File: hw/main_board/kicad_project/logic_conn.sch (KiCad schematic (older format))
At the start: 12 parts, among them P6 CONN_20X2, P8 CONN_12, U8 MAX3002, U9 MAX3002

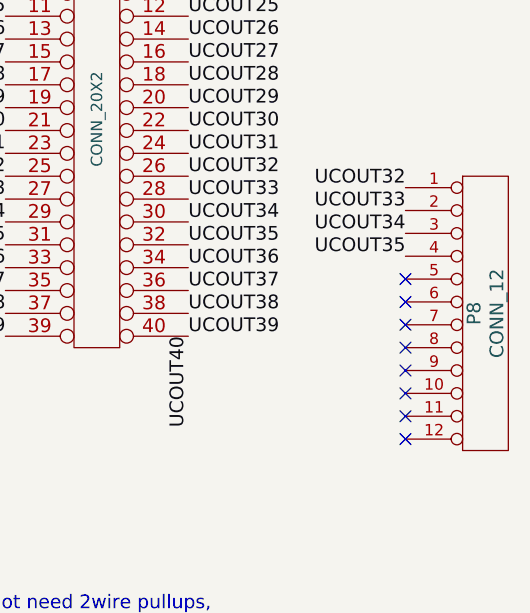
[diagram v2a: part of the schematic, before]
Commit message: final rework of mux board, finalizing stacking connectors, almost there
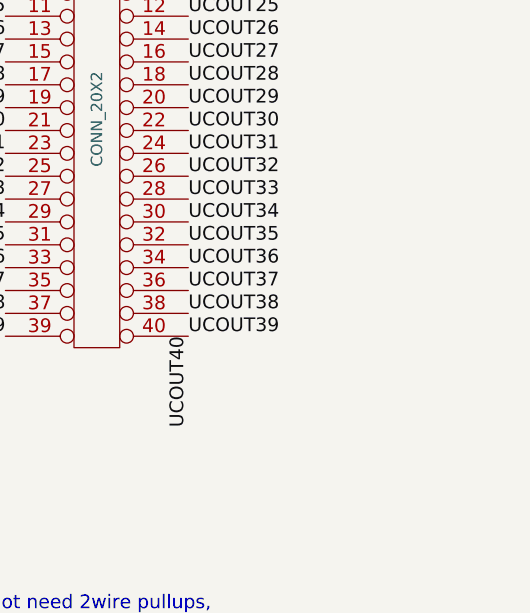
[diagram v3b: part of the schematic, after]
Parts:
- removed P8: CONN_12, symbol CONN_12
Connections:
- no-connect marks 14 -> 6
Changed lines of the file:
@@
 EESchema Schematic File Version 2
-LIBS:power
-LIBS:device
-LIBS:transistors
-LIBS:conn
-LIBS:linear
-LIBS:regul
-LIBS:74xx
-LIBS:cmos4000
-LIBS:adc-dac
-LIBS:memory
-LIBS:xilinx
-LIBS:special
-LIBS:microcontrollers
-LIBS:dsp
-LIBS:microchip
-LIBS:analog_switches
-LIBS:motorola
-LIBS:texas
-LIBS:intel
-LIBS:audio
-LIBS:interface
-LIBS:digital-audio
-LIBS:philips
-LIBS:display
-LIBS:cypress
-LIBS:siliconi
-LIBS:opto
-LIBS:atmel
-LIBS:contrib
-LIBS:valves
 LIBS:ddslib
-LIBS:demuxcomplib
-LIBS:tdsc-kicad-convert
 LIBS:tDCS_driver-cache
 EELAYER 24 0
@@
 $EndComp
 $Comp
-L DVDD_2V5 #PWR08
+L DVDD_2V5 #PWR014
 U 1 1 5245D941
 P 3300 4300
-F 0 "#PWR08" H 3300 4400 30  0001 C CNN
+F 0 "#PWR014" H 3300 4400 30  0001 C CNN
 F 1 "DVDD_2V5" H 3300 4410 30  0000 C CNN
 F 2 "" H 3300 4300 60  0001 C CNN
@@
 $EndComp
 $Comp
-L AGND #PWR09
+L AGND #PWR015
 U 1 1 5245D93C
 P 3000 4650
-F 0 "#PWR09" H 3000 4650 40  0001 C CNN
+F 0 "#PWR015" H 3000 4650 40  0001 C CNN
 F 1 "AGND" H 3000 4580 50  0000 C CNN
 F 2 "" H 3000 4650 60  0001 C CNN
@@
 $EndComp
 $Comp
-L DGND #PWR010
+L DGND #PWR016
 U 1 1 5245D93B
 P 3950 4650
-F 0 "#PWR010" H 3950 4650 40  0001 C CNN
+F 0 "#PWR016" H 3950 4650 40  0001 C CNN
 F 1 "DGND" H 3950 4580 40  0000 C CNN
 F 2 "" H 3950 4650 60  0001 C CNN
@@
 $EndComp
 $Comp
-L AGND #PWR011
+L AGND #PWR017
 U 1 1 5245D93A
 P 3500 2700
-F 0 "#PWR011" H 3500 2700 40  0001 C CNN
+F 0 "#PWR017" H 3500 2700 40  0001 C CNN
 F 1 "AGND" H 3500 2630 50  0000 C CNN
 F 2 "" H 3500 2700 60  0001 C CNN
@@
 $EndComp
 $Comp
-L DVDD_3V3 #PWR012
+L DVDD_3V3 #PWR018
 U 1 1 5245D939
 P 4500 4200
-F 0 "#PWR012" H 4500 4300 30  0001 C CNN
+F 0 "#PWR018" H 4500 4300 30  0001 C CNN
 F 1 "DVDD_3V3" H 4500 4310 30  0000 C CNN
 F 2 "" H 4500 4200 60  0001 C CNN
@@
 MUXC[0..4]
 $Comp
-L DVDD_3V3 #PWR013
+L DVDD_3V3 #PWR019
 U 1 1 523C1EE9
 P 4450 1000
-F 0 "#PWR013" H 4450 1100 30  0001 C CNN
+F 0 "#PWR019" H 4450 1100 30  0001 C CNN
 F 1 "DVDD_3V3" H 4450 1110 30  0000 C CNN
 F 2 "" H 4450 1000 60  0001 C CNN
@@
 $EndComp
 $Comp
-L AGND #PWR014
+L AGND #PWR020
 U 1 1 523C1EBE
 P 3500 2450
-F 0 "#PWR014" H 3500 2450 40  0001 C CNN
+F 0 "#PWR020" H 3500 2450 40  0001 C CNN
 F 1 "AGND" H 3500 2380 50  0000 C CNN
 F 2 "" H 3500 2450 60  0001 C CNN
@@
 $EndComp
 $Comp
-L DGND #PWR015
+L DGND #PWR021
 U 1 1 523C1EBD
 P 3900 550
-F 0 "#PWR015" H 3900 550 40  0001 C CNN
+F 0 "#PWR021" H 3900 550 40  0001 C CNN
 F 1 "DGND" H 3900 480 40  0000 C CNN
 F 2 "" H 3900 550 60  0001 C CNN
@@
 $EndComp
 $Comp
-L AGND #PWR016
+L AGND #PWR022
 U 1 1 523C1EBC
 P 2950 550
-F 0 "#PWR016" H 2950 550 40  0001 C CNN
+F 0 "#PWR022" H 2950 550 40  0001 C CNN
 F 1 "AGND" H 2950 480 50  0000 C CNN
 F 2 "" H 2950 550 60  0001 C CNN
@@
 $EndComp
 $Comp
-L DVDD_2V5 #PWR017
+L DVDD_2V5 #PWR023
 U 1 1 523C1EB7
 P 3250 900
-F 0 "#PWR017" H 3250 1000 30  0001 C CNN
+F 0 "#PWR023" H 3250 1000 30  0001 C CNN
 F 1 "DVDD_2V5" H 3250 1010 30  0000 C CNN
 F 2 "" H 3250 900 60  0001 C CNN
@@
 	1    0    0    -1
 $EndComp
-$Comp
-L CONN_12 P8
-U 1 1 53198391
-P 10750 2400
-F 0 "P8" V 10700 2400 60  0000 C CNN
-F 1 "CONN_12" V 10800 2400 60  0000 C CNN
-F 2 "" H 10750 2400 60  0000 C CNN
-F 3 "" H 10750 2400 60  0000 C CNN
-	1    10750 2400
-	1    0    0    -1
-$EndComp
-Text Label 10400 1850 2    60   ~ 0
-UCOUT32
-Text Label 10400 1950 2    60   ~ 0
-UCOUT33
-Text Label 10400 2050 2    60   ~ 0
-UCOUT34
-Text Label 10400 2150 2    60   ~ 0
-UCOUT35
-NoConn ~ 10400 2250
-NoConn ~ 10400 2350
-NoConn ~ 10400 2450
-NoConn ~ 10400 2550
-NoConn ~ 10400 2650
-NoConn ~ 10400 2750
-NoConn ~ 10400 2850
-NoConn ~ 10400 2950
 Text Label 7150 4300 2    60   ~ 0
 RNG_0

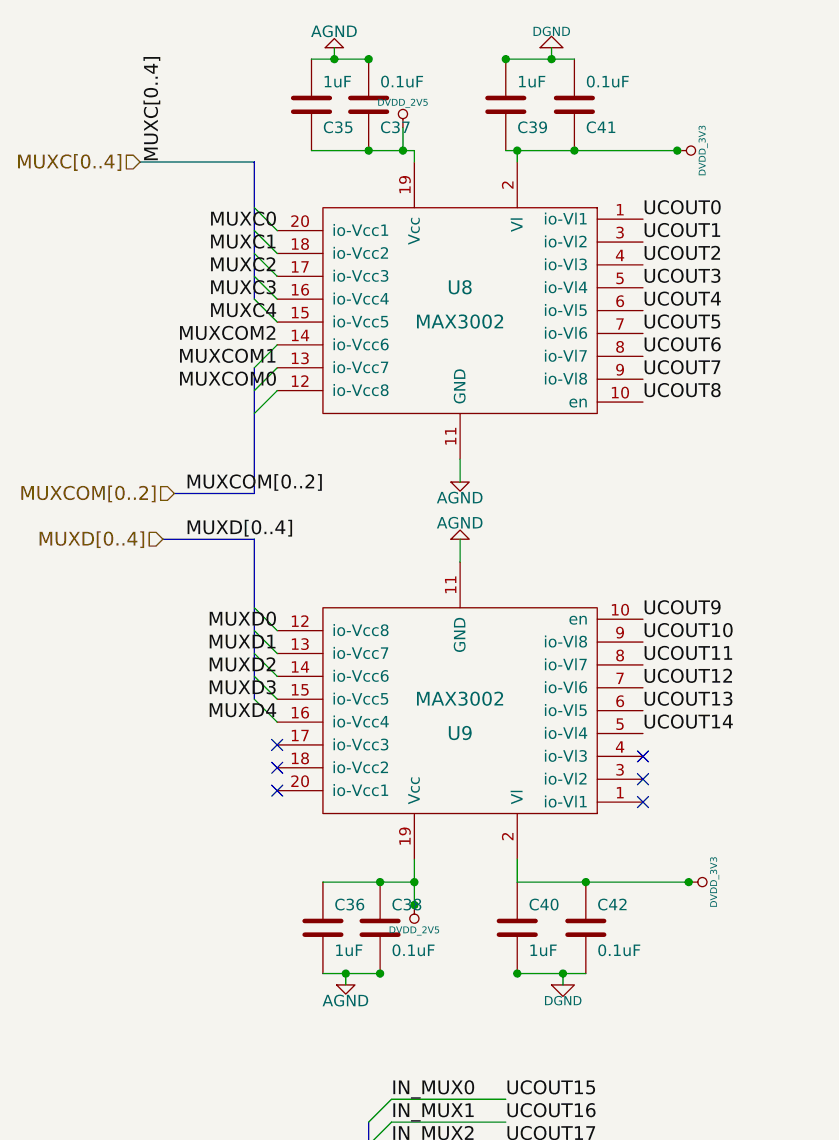
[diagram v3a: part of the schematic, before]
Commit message: finished component layout on mainboard, need to route power planes and the digital control signal lines
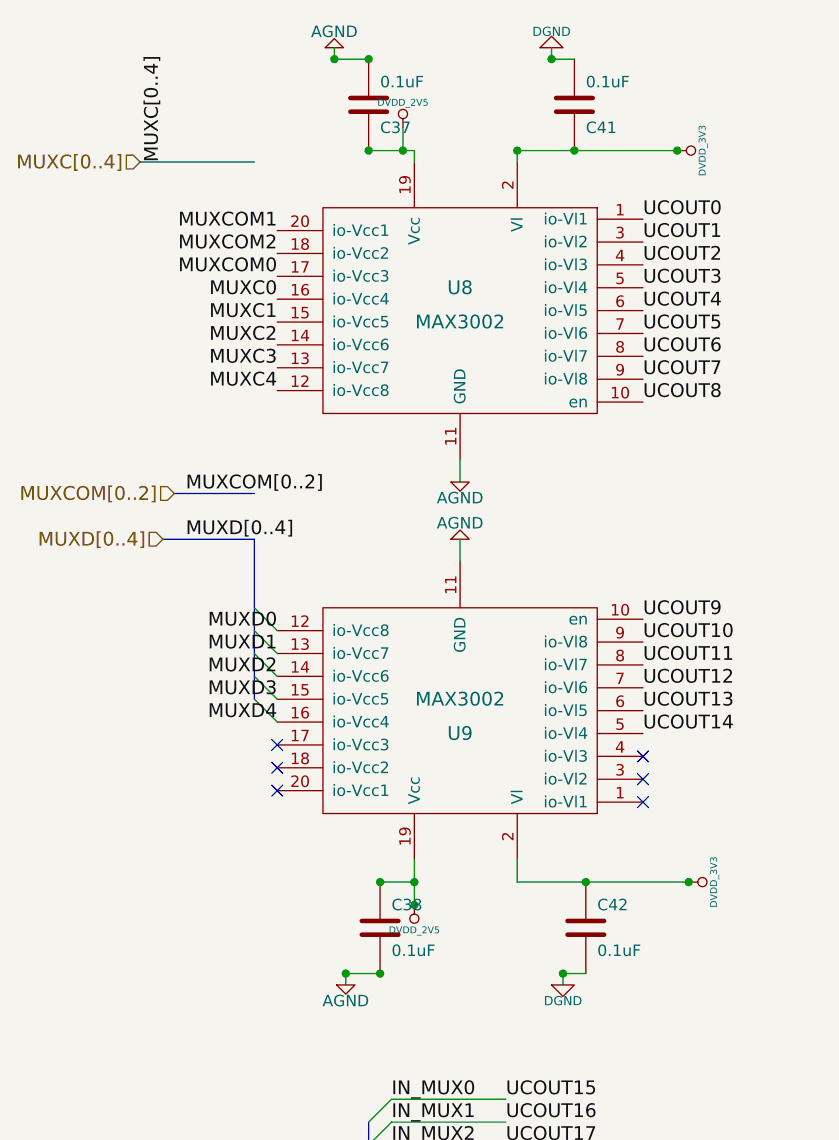
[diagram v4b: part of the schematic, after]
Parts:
- removed C35, C36, C39, C40: 1uF, 0603, symbol C
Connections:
- net MUXC0: now also U8.16 (io-Vcc4); no longer U8.20 (io-Vcc1)
- net MUXC1: now also U8.15 (io-Vcc5); no longer U8.18 (io-Vcc2)
- net MUXC2: now also U8.14 (io-Vcc6); no longer U8.17 (io-Vcc3)
- net MUXC3: now also U8.13 (io-Vcc7); no longer U8.16 (io-Vcc4)
- net MUXC4: now also U8.12 (io-Vcc8); no longer U8.15 (io-Vcc5)
- net MUXCOM0: now also U8.17 (io-Vcc3); no longer U8.12 (io-Vcc8)
- net MUXCOM1: now also U8.20 (io-Vcc1); no longer U8.13 (io-Vcc7)
- net MUXCOM2: now also U8.18 (io-Vcc2); no longer U8.14 (io-Vcc6)
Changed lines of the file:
@@
 EESchema Schematic File Version 2
 LIBS:ddslib
+LIBS:demuxcomplib
 LIBS:tDCS_driver-cache
 EELAYER 24 0
@@
 Wire Wire Line
 	3950 4600 3950 4650
-Connection ~ 3750 4600
 Connection ~ 3150 4600
 Connection ~ 3300 4200
@@
 Wire Wire Line
 	3000 4600 3000 4650
-Wire Wire Line
-	3300 4200 2900 4200
 Connection ~ 3150 4200
-Wire Wire Line
-	2900 4600 3150 4600
-Wire Wire Line
-	4050 4600 3750 4600
 Connection ~ 3950 4600
 Wire Wire Line
@@
 Wire Bus Line
 	2100 1050 2600 1050
-Wire Bus Line
-	2600 1050 2600 1650
 Connection ~ 3900 600
-Wire Wire Line
-	4000 600  3700 600
-Wire Wire Line
-	2850 600  3100 600
 Connection ~ 3100 1000
 Wire Wire Line
@@
 Connection ~ 3250 1000
 Connection ~ 3100 600
-Connection ~ 3700 600
 Wire Wire Line
 	3900 600  3900 550
-Wire Wire Line
-	3700 1000 4450 1000
 Connection ~ 4000 1000
 Wire Bus Line
 	2250 2500 2600 2500
-Wire Bus Line
-	2600 2500 2600 1950
-Wire Wire Line
-	2850 1000 3300 1000
 Wire Wire Line
 	3300 1000 3300 1050
@@
 $EndComp
 $Comp
-L DVDD_2V5 #PWR014
+L DVDD_2V5 #PWR013
 U 1 1 5245D941
 P 3300 4300
-F 0 "#PWR014" H 3300 4400 30  0001 C CNN
+F 0 "#PWR013" H 3300 4400 30  0001 C CNN
 F 1 "DVDD_2V5" H 3300 4410 30  0000 C CNN
 F 2 "" H 3300 4300 60  0001 C CNN
@@
 $EndComp
 $Comp
-L C C36
-U 1 1 5245D93F
-P 2900 4400
-F 0 "C36" H 2950 4500 50  0000 L CNN
-F 1 "1uF" H 2950 4300 50  0000 L CNN
-F 2 "0603" H 2900 4400 60  0001 C CNN
-F 3 "" H 2900 4400 60  0001 C CNN
-	1    2900 4400
-	1    0    0    -1
-$EndComp
-$Comp
 L C C42
 U 1 1 5245D93E
@@
 $EndComp
 $Comp
-L C C40
-U 1 1 5245D93D
-P 3750 4400
-F 0 "C40" H 3800 4500 50  0000 L CNN
-F 1 "1uF" H 3800 4300 50  0000 L CNN
-F 2 "0603" H 3750 4400 60  0001 C CNN
-F 3 "" H 3750 4400 60  0001 C CNN
-	1    3750 4400
-	1    0    0    -1
-$EndComp
-$Comp
-L AGND #PWR015
+L AGND #PWR014
 U 1 1 5245D93C
 P 3000 4650
-F 0 "#PWR015" H 3000 4650 40  0001 C CNN
+F 0 "#PWR014" H 3000 4650 40  0001 C CNN
 F 1 "AGND" H 3000 4580 50  0000 C CNN
 F 2 "" H 3000 4650 60  0001 C CNN
@@
 $EndComp
 $Comp
-L DGND #PWR016
+L DGND #PWR015
 U 1 1 5245D93B
 P 3950 4650
-F 0 "#PWR016" H 3950 4650 40  0001 C CNN
+F 0 "#PWR015" H 3950 4650 40  0001 C CNN
 F 1 "DGND" H 3950 4580 40  0000 C CNN
 F 2 "" H 3950 4650 60  0001 C CNN
@@
 $EndComp
 $Comp
-L AGND #PWR017
+L AGND #PWR016
 U 1 1 5245D93A
 P 3500 2700
-F 0 "#PWR017" H 3500 2700 40  0001 C CNN
+F 0 "#PWR016" H 3500 2700 40  0001 C CNN
 F 1 "AGND" H 3500 2630 50  0000 C CNN
 F 2 "" H 3500 2700 60  0001 C CNN
@@
 $EndComp
 $Comp
-L DVDD_3V3 #PWR018
+L DVDD_3V3 #PWR017
 U 1 1 5245D939
 P 4500 4200
-F 0 "#PWR018" H 4500 4300 30  0001 C CNN
+F 0 "#PWR017" H 4500 4300 30  0001 C CNN
 F 1 "DVDD_3V3" H 4500 4310 30  0000 C CNN
 F 2 "" H 4500 4200 60  0001 C CNN
@@
 MUXC[0..4]
 $Comp
-L DVDD_3V3 #PWR019
+L DVDD_3V3 #PWR018
 U 1 1 523C1EE9
 P 4450 1000
-F 0 "#PWR019" H 4450 1100 30  0001 C CNN
+F 0 "#PWR018" H 4450 1100 30  0001 C CNN
 F 1 "DVDD_3V3" H 4450 1110 30  0000 C CNN
 F 2 "" H 4450 1000 60  0001 C CNN
@@
 $EndComp
 $Comp
-L AGND #PWR020
+L AGND #PWR019
 U 1 1 523C1EBE
 P 3500 2450
-F 0 "#PWR020" H 3500 2450 40  0001 C CNN
+F 0 "#PWR019" H 3500 2450 40  0001 C CNN
 F 1 "AGND" H 3500 2380 50  0000 C CNN
 F 2 "" H 3500 2450 60  0001 C CNN
@@
 $EndComp
 $Comp
-L DGND #PWR021
+L DGND #PWR020
 U 1 1 523C1EBD
 P 3900 550
-F 0 "#PWR021" H 3900 550 40  0001 C CNN
+F 0 "#PWR020" H 3900 550 40  0001 C CNN
 F 1 "DGND" H 3900 480 40  0000 C CNN
 F 2 "" H 3900 550 60  0001 C CNN
@@
 $EndComp
 $Comp
-L AGND #PWR022
+L AGND #PWR021
 U 1 1 523C1EBC
 P 2950 550
-F 0 "#PWR022" H 2950 550 40  0001 C CNN
+F 0 "#PWR021" H 2950 550 40  0001 C CNN
 F 1 "AGND" H 2950 480 50  0000 C CNN
 F 2 "" H 2950 550 60  0001 C CNN
 F 3 "" H 2950 550 60  0001 C CNN
 	1    2950 550
-	1    0    0    1
-$EndComp
-$Comp
-L C C39
-U 1 1 523C1EBB
-P 3700 800
-F 0 "C39" H 3750 900 50  0000 L CNN
-F 1 "1uF" H 3750 700 50  0000 L CNN
-F 2 "0603" H 3700 800 60  0001 C CNN
-F 3 "" H 3700 800 60  0001 C CNN
-	1    3700 800
 	1    0    0    1
 $EndComp
@@
 $EndComp
 $Comp
-L C C35
-U 1 1 523C1EB9
-P 2850 800
-F 0 "C35" H 2900 900 50  0000 L CNN
-F 1 "1uF" H 2900 700 50  0000 L CNN
-F 2 "0603" H 2850 800 60  0001 C CNN
-F 3 "" H 2850 800 60  0001 C CNN
-	1    2850 800
-	1    0    0    1
-$EndComp
-$Comp
 L C C37
 U 1 1 523C1EB8
@@
 $EndComp
 $Comp
-L DVDD_2V5 #PWR023
+L DVDD_2V5 #PWR022
 U 1 1 523C1EB7
 P 3250 900
-F 0 "#PWR023" H 3250 1000 30  0001 C CNN
+F 0 "#PWR022" H 3250 1000 30  0001 C CNN
 F 1 "DVDD_2V5" H 3250 1010 30  0000 C CNN
 F 2 "" H 3250 900 60  0001 C CNN
@@
 	-1   0    0    -1
 $EndComp
+Text Label 2700 1650 2    60   ~ 0
+MUXC0
+Text Label 2700 1750 2    60   ~ 0
+MUXC1
+Text Label 2700 1850 2    60   ~ 0
+MUXC2
+Text Label 2700 1950 2    60   ~ 0
+MUXC3
+Text Label 2700 2050 2    60   ~ 0
+MUXC4
+Text Label 2700 1550 2    60   ~ 0
+MUXCOM0
 Text Label 2700 1350 2    60   ~ 0
-MUXC0
+MUXCOM1
 Text Label 2700 1450 2    60   ~ 0
-MUXC1
-Text Label 2700 1550 2    60   ~ 0
-MUXC2
-Text Label 2700 1650 2    60   ~ 0
-MUXC3
-Text Label 2700 1750 2    60   ~ 0
-MUXC4
-Entry Wire Line
-	2600 1250 2700 1350
-Entry Wire Line
-	2600 1350 2700 1450
-Entry Wire Line
-	2600 1450 2700 1550
-Entry Wire Line
-	2600 1550 2700 1650
-Entry Wire Line
-	2600 1650 2700 1750
-Text Label 2700 2050 2    60   ~ 0
-MUXCOM0
-Text Label 2700 1950 2    60   ~ 0
-MUXCOM1
-Text Label 2700 1850 2    60   ~ 0
 MUXCOM2
-Entry Wire Line
-	2600 1950 2700 1850
-Entry Wire Line
-	2600 2050 2700 1950
-Entry Wire Line
-	2600 2150 2700 2050
 Text Notes 9550 3900 2    60   ~ 0
 Does not need 2wire pullups, \npulldowns needed for default\n on sleep/pselect/fselect (bit 6,7,9)
@@
 Text Label 7150 4600 2    60   ~ 0
 RNG_3
+Wire Wire Line
+	2950 600  3100 600
+Wire Wire Line
+	3100 1000 3300 1000
+Wire Wire Line
+	3750 1000 4450 1000
+Wire Wire Line
+	4000 600  3900 600
+Wire Wire Line
+	3950 4600 4050 4600
+Wire Wire Line
+	3000 4600 3150 4600
+Wire Wire Line
+	3150 4200 3300 4200
 $EndSCHEMATC

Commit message: Converting keepnote notes to thorough design documentation, starting with BRD1
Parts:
- removed P6: CONN_20X2, symbol CONN_20X2
- added P6: CONN_25X2, symbol CONN_25X2
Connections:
- net labels added: UCOUT41, UCOUT42, UCOUT43, UCOUT44, UCOUT45, UCOUT46, UCOUT47, UCOUT48, UCOUT49
- no-connect marks 6 -> 7
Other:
- moved on the sheet: C37, C38, C41, C42, U8
